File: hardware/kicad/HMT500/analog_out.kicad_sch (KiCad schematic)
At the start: 20 parts, among them U10 TPS26611, U7 DAC8760IPWP, U8 DAC8760IPWP, U9 TPS26611

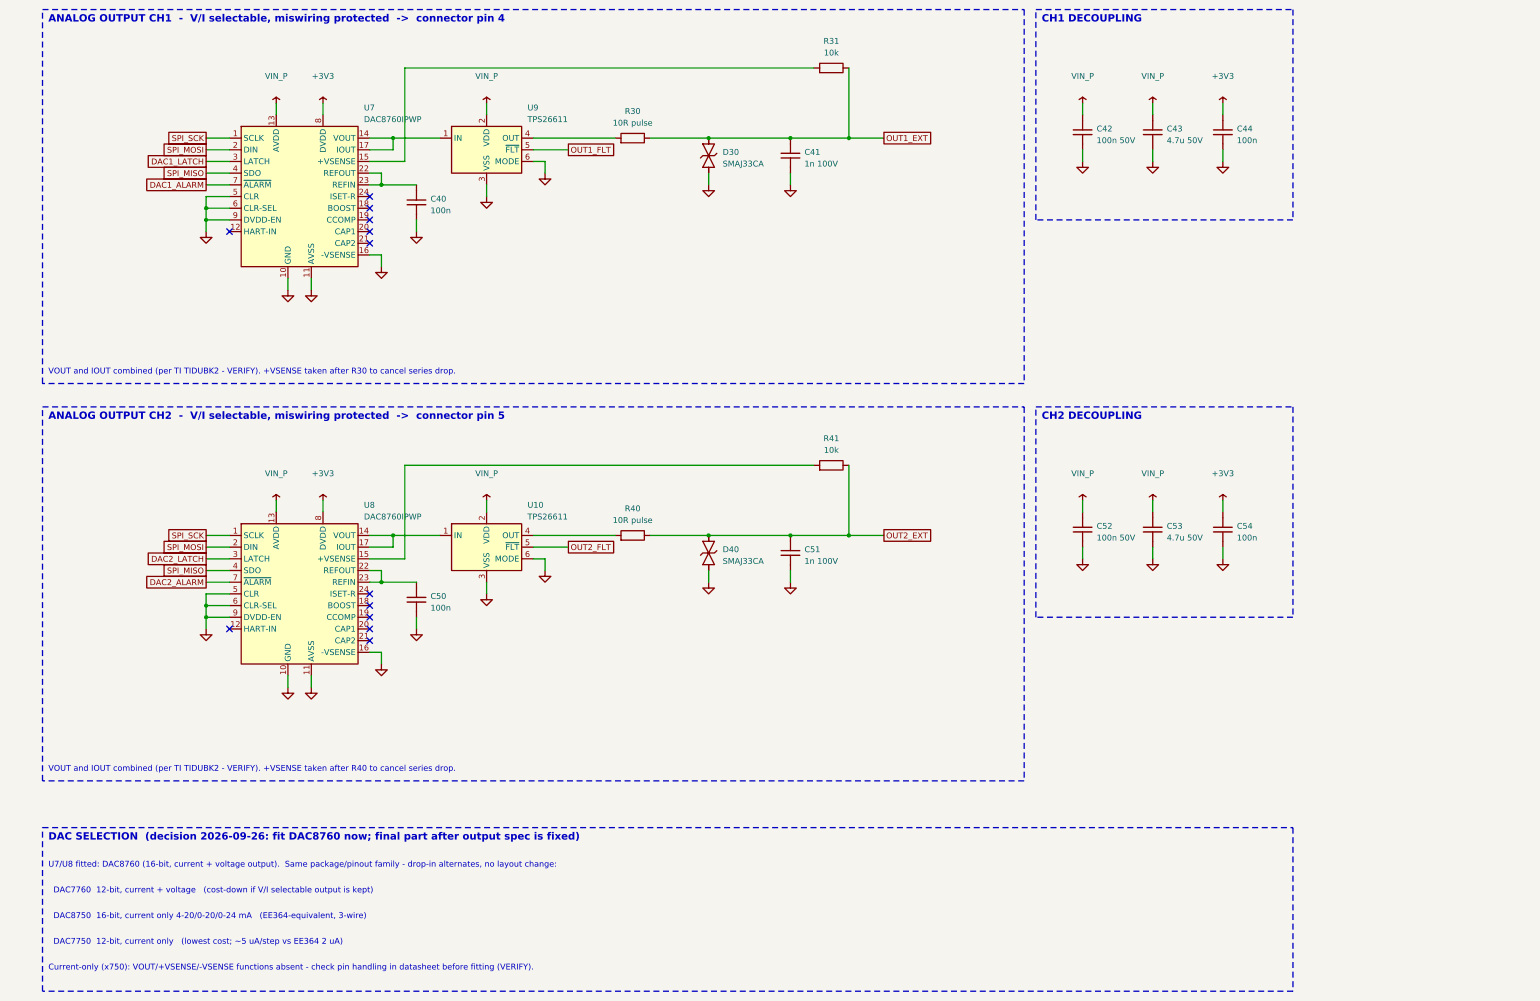
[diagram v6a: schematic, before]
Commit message: Schematic drawing rules: no overlapping text, Korean font, distinct net names
- Generator places reference/value text automatically, clear of symbol bodies,
  pins, wires, labels, notes and box edges; validation fails on any overlap
  (also note text vs wires/power names and bodies vs box edges)
- Fix 180-degree parts (LED) whose justification KiCad mirrors
- Styles: reference bold, value normal, power nets italic, signal nets boxed labels
- Korean box subtitles and legend in NanumGothic TrueType (stroke font has no Hangul)
- Nets renamed where they matched part or pin names: LED -> STAT_LED, EF_ILIM/IMON/DVDT
- J1 GH mounting pads removed from the symbol (PCB only); connector sheet re-spaced
- Schematic PDF export added; tests for net naming and Hangul font

Co-Authored-By: Claude Opus 5.5 <noreply@anthropic.com>
Claude-Session: https://claude.ai/code/session_01JA2o8uJsqp9Vzsg4b665ev
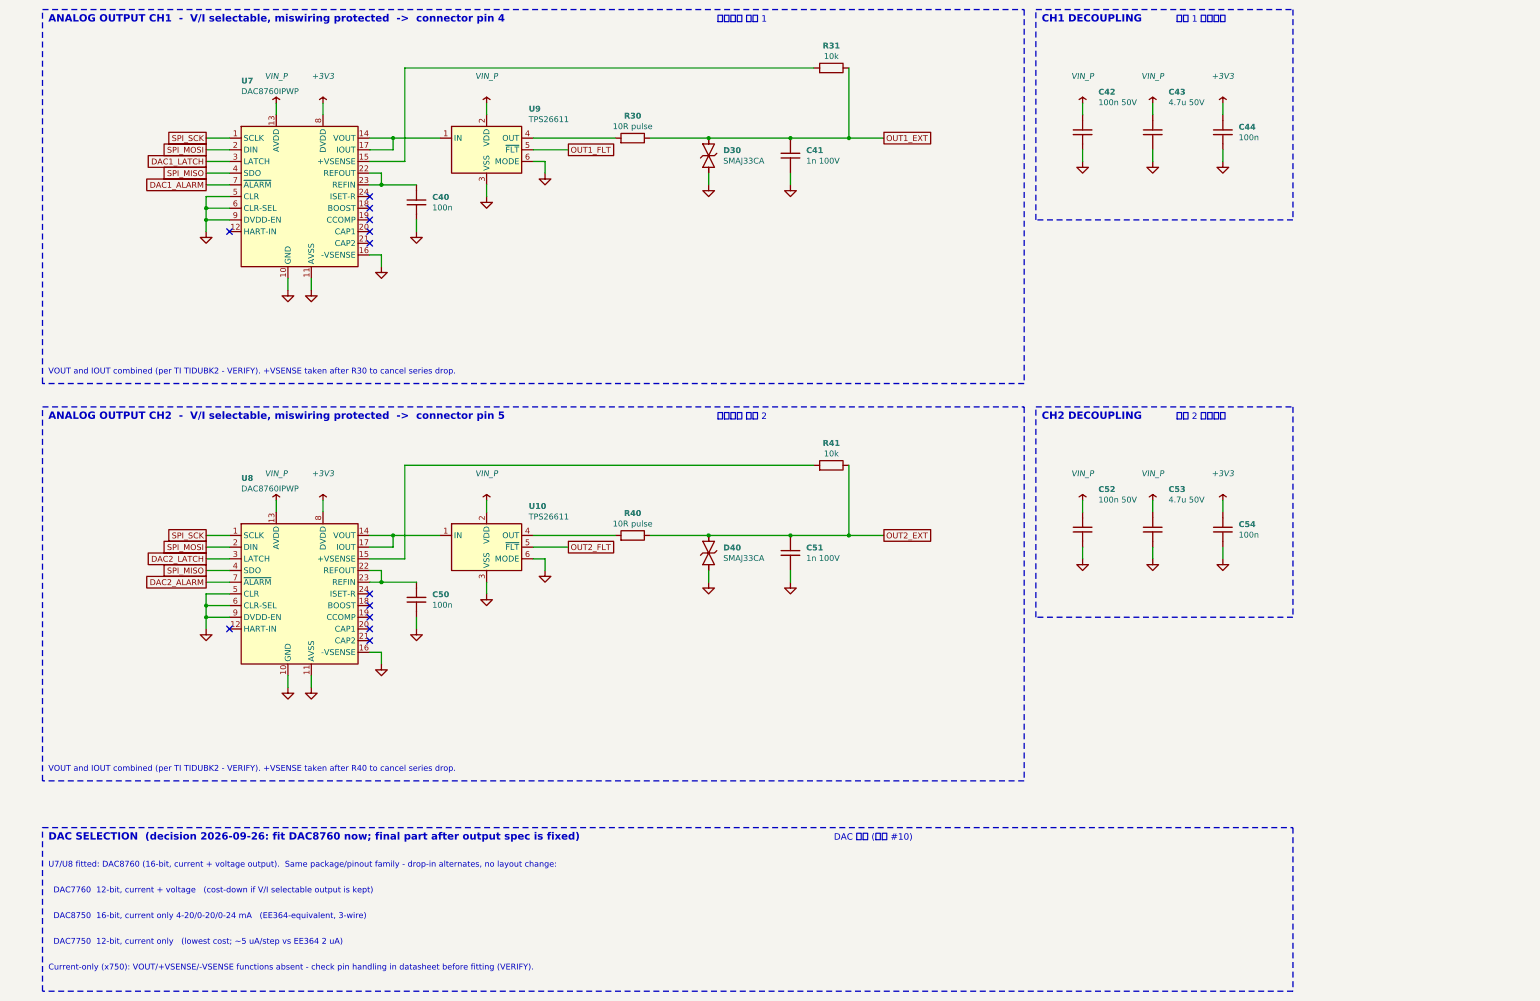
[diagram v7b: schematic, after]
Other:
- note added: "DAC 선정 (결정 #10)"
- note added: "아날로그 출력 1"
- note added: "아날로그 출력 2"
- note added: "채널 1 바이패스"
- note added: "채널 2 바이패스"
